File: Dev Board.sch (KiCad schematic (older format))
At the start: 2 parts

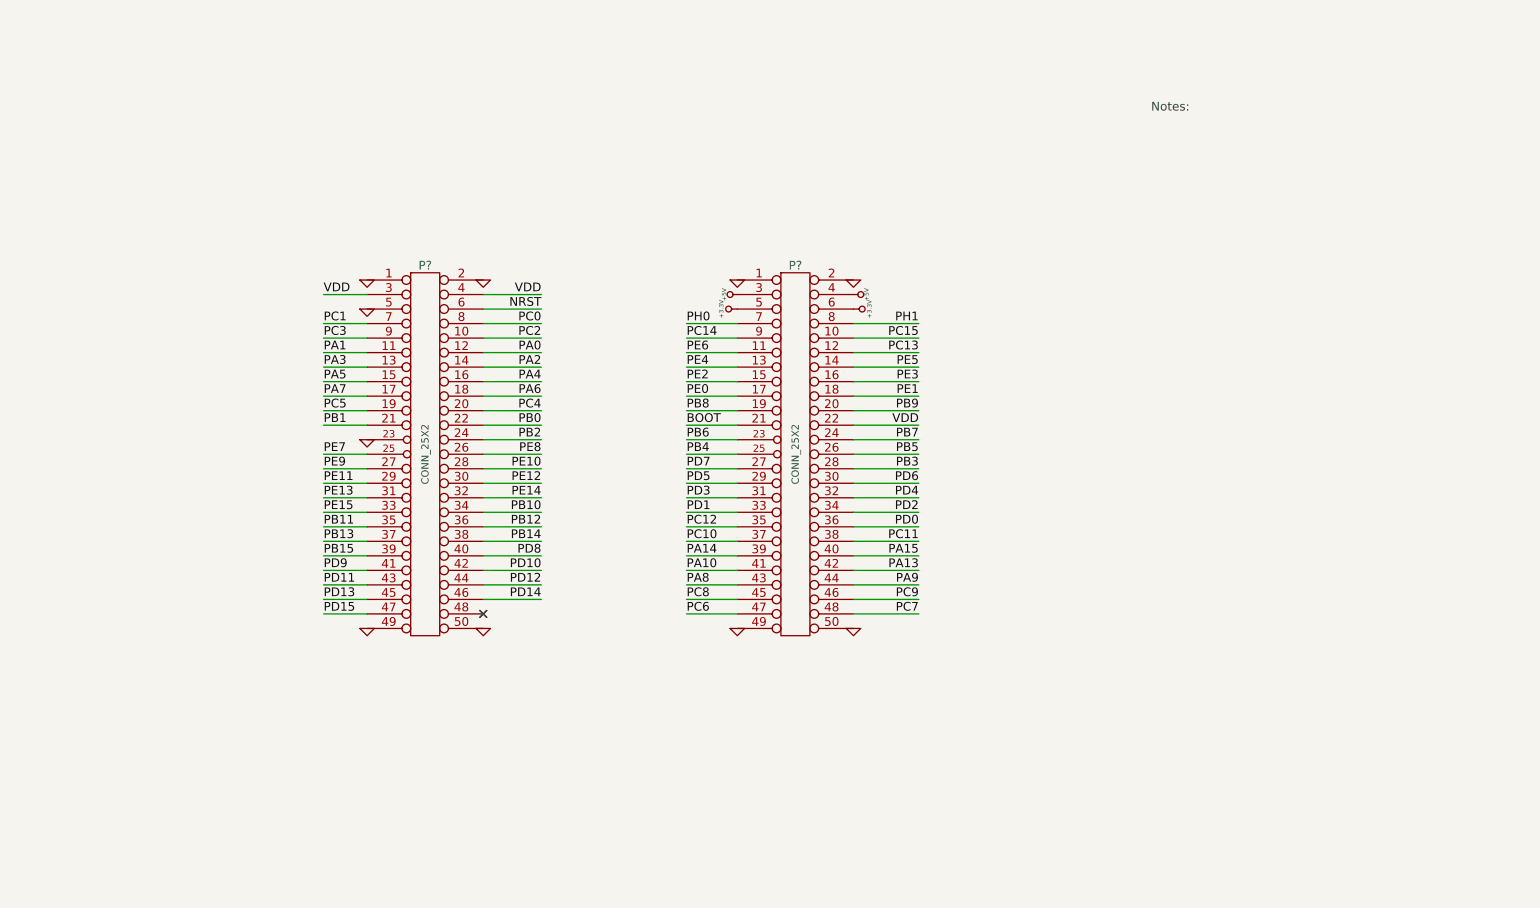
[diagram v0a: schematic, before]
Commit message: Added some more of the connectors to the Dev Board.  Will work through the camera, spi, i2c and cans interfaces next
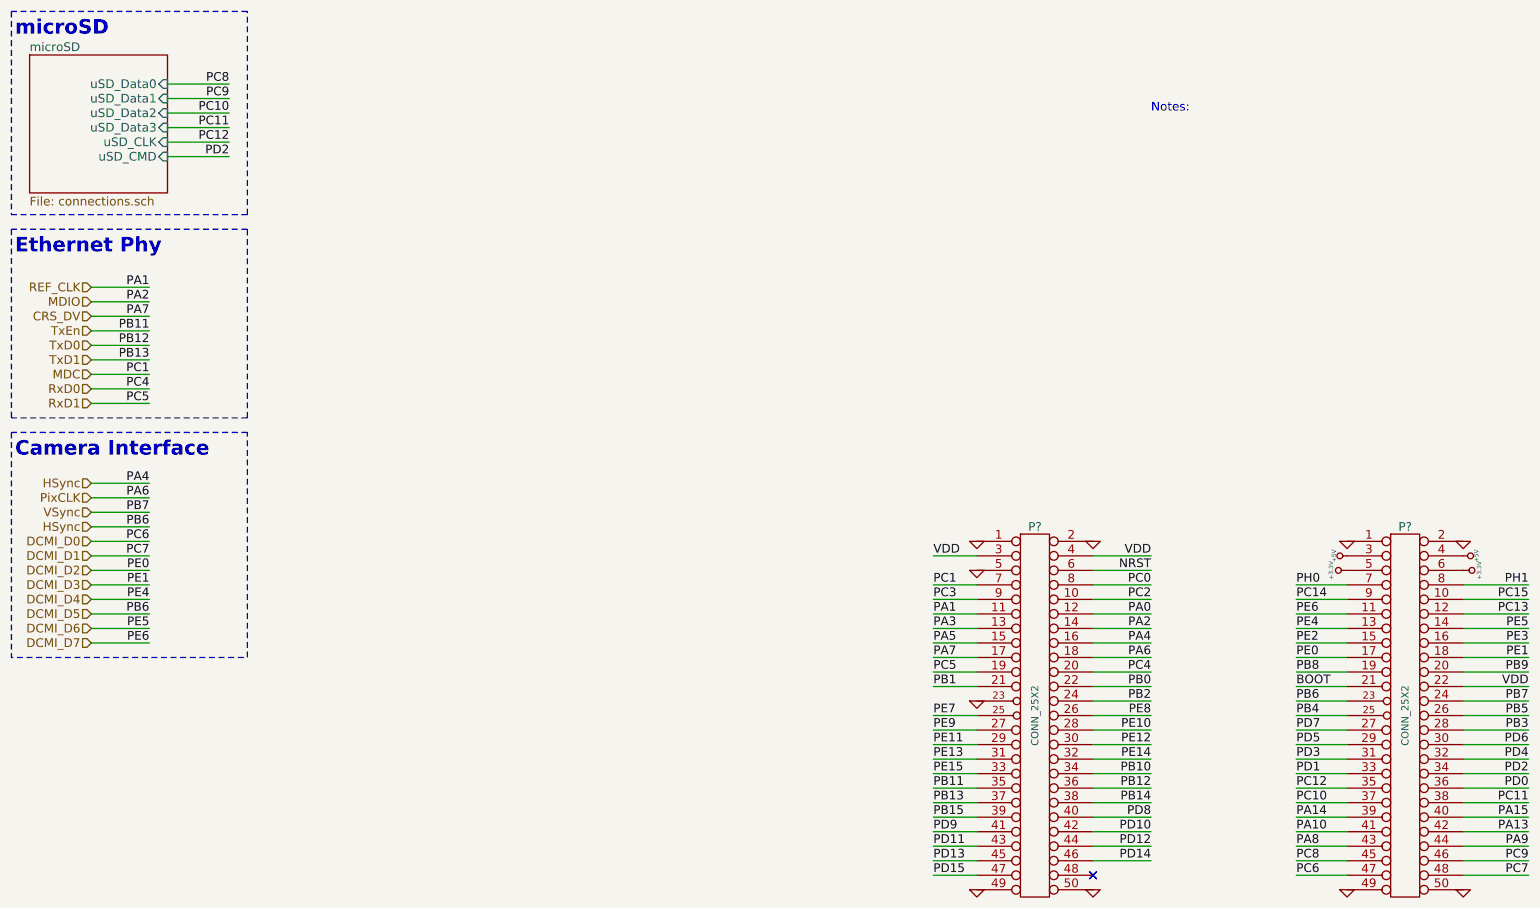
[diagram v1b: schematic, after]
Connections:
- net PB6 is gone; now on net DCMI_D5: P?.23 (P23)
- net PA1 renamed REF_CLK
- net PA2 renamed MDIO
- net PA4 renamed DCMI_D5
- net PA6 renamed PixCLK
- net PA7 renamed CRS_DV
- net PB11 renamed TxEn
- net PB12 renamed TxD0
- net PB13 renamed TxD1
- net PB7 renamed VSync
- net PC1 renamed MDC
- net PC4 renamed RxD0
- net PC5 renamed RxD1
- net PC6 renamed DCMI_D0
- net PC7 renamed DCMI_D1
- net PE0 renamed DCMI_D2
- net PE1 renamed DCMI_D3
- net PE4 renamed DCMI_D4
- net PE5 renamed DCMI_D6
- net PE6 renamed DCMI_D7
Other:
- note added: "Camera Interface"
- note added: "Ethernet Phy"
- note added: "microSD"
- moved on the sheet: P?
